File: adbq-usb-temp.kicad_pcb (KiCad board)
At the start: 4 copper layers, 0 parts

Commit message: pcb: import footprints from schematic
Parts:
- added AE1: Antenna, RF_Antenna:Johanson_2450AT18x100, F.Cu at (155.2, 88.0)
- added C1: 1u, Capacitor_SMD:C_0402_1005Metric, F.Cu at (137.8, 93.2)
- added C10: 0u1, Capacitor_SMD:C_0402_1005Metric, F.Cu at (140.7, 97.1)
- added C11: 0u1, Capacitor_SMD:C_0402_1005Metric, F.Cu at (140.7, 99.1)
- added C13: 10n, Capacitor_SMD:C_0402_1005Metric, F.Cu at (140.7, 101.1)
- added C14: 1u, Capacitor_SMD:C_0402_1005Metric, F.Cu at (140.7, 103.1)
- added C15: 1u, Capacitor_SMD:C_0402_1005Metric, F.Cu at (143.5, 93.2)
- added C16: 0u1, Capacitor_SMD:C_0402_1005Metric, F.Cu at (143.5, 95.2)
- added C17: 0u1, Capacitor_SMD:C_0402_1005Metric, F.Cu at (143.5, 97.1)
- added C18: 0u1, Capacitor_SMD:C_0402_1005Metric, F.Cu at (143.5, 99.1)
- added C2: 10u, Capacitor_SMD:C_0402_1005Metric, F.Cu at (137.8, 95.2)
- added C23: 12p, Capacitor_SMD:C_0402_1005Metric, F.Cu at (143.5, 101.1)
- added C25: 12p, Capacitor_SMD:C_0402_1005Metric, F.Cu at (143.5, 103.1)
- added C28: 1p2, Capacitor_SMD:C_0402_1005Metric, F.Cu at (146.4, 93.2)
- added C29: 1p2, Capacitor_SMD:C_0402_1005Metric, F.Cu at (146.4, 95.2)
- added C3: 10u, Capacitor_SMD:C_0402_1005Metric, F.Cu at (137.8, 97.1)
- added C4: 10u, Capacitor_SMD:C_0402_1005Metric, F.Cu at (137.8, 99.1)
- added C48: 0u1, Capacitor_SMD:C_0402_1005Metric, F.Cu at (146.4, 97.1)
- added C5: 100p, Capacitor_SMD:C_0402_1005Metric, F.Cu at (137.8, 101.1)
- added C52: 1p, Capacitor_SMD:C_0402_1005Metric, F.Cu at (146.4, 99.1)
- added C6: 0u1, Capacitor_SMD:C_0402_1005Metric, F.Cu at (137.8, 103.1)
- added C8: 10u, Capacitor_SMD:C_0402_1005Metric, F.Cu at (140.7, 93.2)
- added C9: 1u, Capacitor_SMD:C_0402_1005Metric, F.Cu at (140.7, 95.2)
- added D1: H5VU10U, Pers:Diode_DFN1006, F.Cu at (157.4, 103.7)
- added D2: H5VU10U, Pers:Diode_DFN1006, F.Cu at (157.4, 105.7)
- added D3: H5VU10U, Pers:Diode_DFN1006, F.Cu at (157.4, 107.7)
- added J4: USB_C_Receptacle_USB2.0_14P, Connector_USB:USB_C_Receptacle_HRO_TYPE-C-31-M-12, F.Cu at (153.7, 98.0)
- added JP1: Jumper_2_Open, Jumper:SolderJumper-2_P1.3mm_Open_RoundedPad1.0x1.5mm, F.Cu at (154.5, 80.9)
- added L1: 0u47, Pers:TDK_TFM201610ALC, F.Cu at (127.0, 109.7)
- added L2: 2n7, Inductor_SMD:L_0402_1005Metric, F.Cu at (126.2, 93.2)
- added L3: 24n, Inductor_SMD:L_0402_1005Metric, F.Cu at (126.2, 95.2)
- added L4: 2n7, Inductor_SMD:L_0402_1005Metric, F.Cu at (126.2, 97.2)
- added L6: 3n9, Inductor_SMD:L_0402_1005Metric, F.Cu at (126.2, 99.2)
- added L7: 2n7, Inductor_SMD:L_0402_1005Metric, F.Cu at (126.2, 101.2)
- added Q1: Q_NMOS, Package_TO_SOT_SMD:SOT-323_SC-70, F.Cu at (150.1, 104.7)
- added Q2: Q_NMOS, Package_TO_SOT_SMD:SOT-323_SC-70, F.Cu at (150.1, 108.6)
- added Q3: Q_NMOS, Package_TO_SOT_SMD:SOT-323_SC-70, F.Cu at (150.1, 112.4)
- added R1: 10k, Resistor_SMD:R_0402_1005Metric, F.Cu at (126.2, 103.2)
- added R10: 22, Resistor_SMD:R_0402_1005Metric, F.Cu at (129.1, 103.2)
- added R11: 510, Resistor_SMD:R_0402_1005Metric, F.Cu at (129.1, 105.2)
- added R12: 5k1, Resistor_SMD:R_0402_1005Metric, F.Cu at (129.1, 107.1)
- added R13: 5k1, Resistor_SMD:R_0402_1005Metric, F.Cu at (132.0, 93.2)
- added R14: 22, Resistor_SMD:R_0402_1005Metric, F.Cu at (132.0, 95.2)
- added R15: 510, Resistor_SMD:R_0402_1005Metric, F.Cu at (132.0, 97.2)
- added R16: 150, Resistor_SMD:R_0402_1005Metric, F.Cu at (132.0, 99.2)
- added R17: 150, Resistor_SMD:R_0402_1005Metric, F.Cu at (132.0, 101.2)
- added R18: 150, Resistor_SMD:R_0402_1005Metric, F.Cu at (132.0, 103.2)
- added R19: 150, Resistor_SMD:R_0402_1005Metric, F.Cu at (132.0, 105.2)
- added R2: 10k, Resistor_SMD:R_0402_1005Metric, F.Cu at (126.2, 105.2)
- added R20: 150, Resistor_SMD:R_0402_1005Metric, F.Cu at (132.0, 107.1)
- added R21: 150, Resistor_SMD:R_0402_1005Metric, F.Cu at (134.9, 93.2)
- added R22: 150, Resistor_SMD:R_0402_1005Metric, F.Cu at (134.9, 95.2)
- added R23: 150, Resistor_SMD:R_0402_1005Metric, F.Cu at (134.9, 97.2)
- added R24: 10k, Resistor_SMD:R_0402_1005Metric, F.Cu at (134.9, 99.2)
- added R25: 20k, Resistor_SMD:R_0402_1005Metric, F.Cu at (134.9, 101.2)
- added R26: 20k, Resistor_SMD:R_0402_1005Metric, F.Cu at (134.9, 103.2)
- added R3: 10k, Resistor_SMD:R_0402_1005Metric, F.Cu at (126.2, 107.1)
- added R4: 430k, Resistor_SMD:R_0603_1608Metric, F.Cu at (126.7, 112.5)
- added R5: 100k, Resistor_SMD:R_0402_1005Metric, F.Cu at (129.1, 93.2)
- added R57: 10k, Resistor_SMD:R_0402_1005Metric, F.Cu at (134.9, 105.2)
- added R6: 510, Resistor_SMD:R_0402_1005Metric, F.Cu at (129.1, 95.2)
- added R7: 510, Resistor_SMD:R_0402_1005Metric, F.Cu at (129.1, 97.2)
- added R8: 510, Resistor_SMD:R_0402_1005Metric, F.Cu at (129.1, 99.2)
- added R9: 510, Resistor_SMD:R_0402_1005Metric, F.Cu at (129.1, 101.2)
- added SW1: SW_Push, Jumper:SolderJumper-2_P1.3mm_Open_RoundedPad1.0x1.5mm, F.Cu at (154.5, 84.5)
- added SW2: TestPoint, TestPoint:TestPoint_Pad_D1.5mm, F.Cu at (154.1, 104.5)
- added SW3: TestPoint, TestPoint:TestPoint_Pad_D1.5mm, F.Cu at (154.1, 108.0)
- added SW4: TestPoint, TestPoint:TestPoint_Pad_D1.5mm, F.Cu at (154.1, 111.6)
- added U1: ESP32-S3FH4R2, Package_DFN_QFN:QFN-56-1EP_7x7mm_P0.4mm_EP5.6x5.6mm, F.Cu at (141.4, 108.7)
- added U14: TMP117AIDRV, Package_SON:WSON-6-1EP_2x2mm_P0.65mm_EP1x1.6mm, F.Cu at (150.4, 84.7)
- added U2: TPS6282x, Pers:Texas_VSON-6_1.5x1.5mm_P0.5mm_DMQ0006A, F.Cu at (157.6, 110.5)
- added U3: XL-SB2301SRWC, Pers:XL-SB2301SRWC, F.Cu at (136.7, 85.7)
- added U4: TMP117AIDRV, Package_SON:WSON-6-1EP_2x2mm_P0.65mm_EP1x1.6mm, F.Cu at (150.4, 81.0)
- added Y1: 48M, Crystal:Crystal_SMD_2016-4Pin_2.0x1.6mm, F.Cu at (131.3, 110.0)

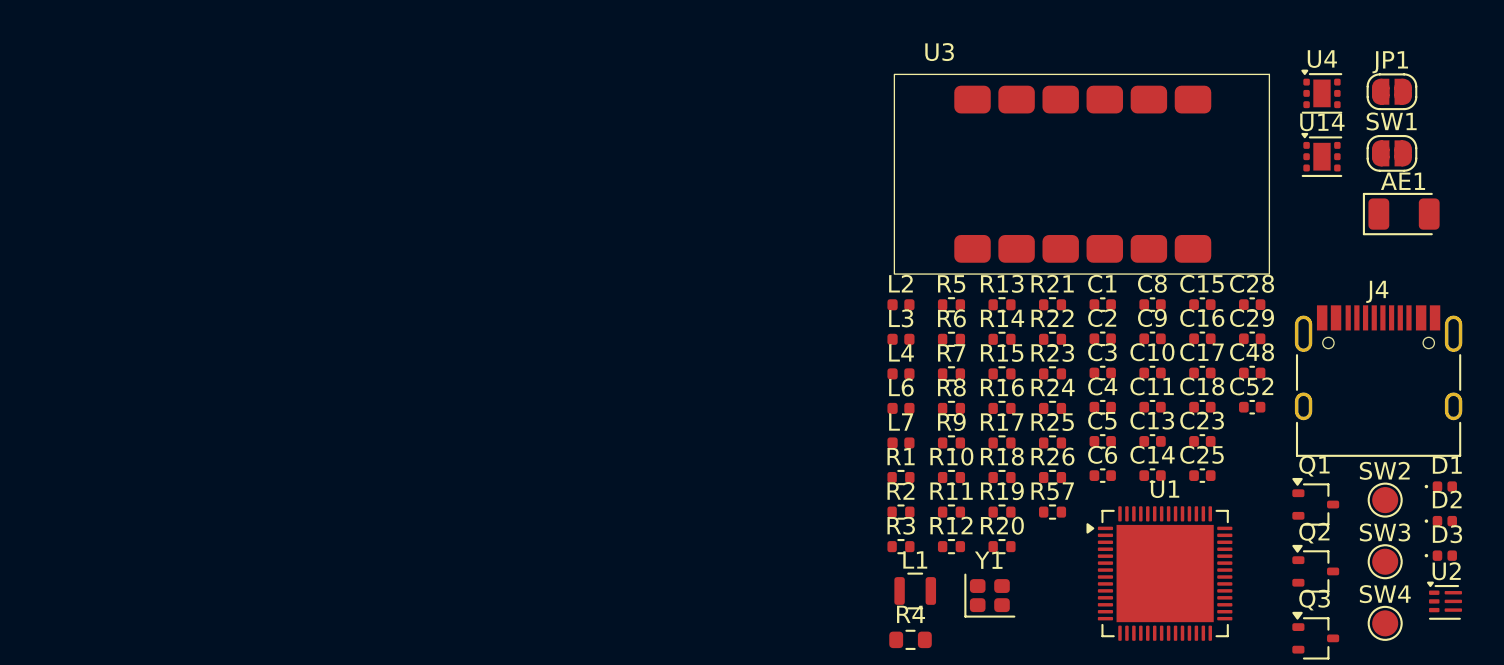
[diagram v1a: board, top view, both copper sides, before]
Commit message: pcb: add missing 3d models
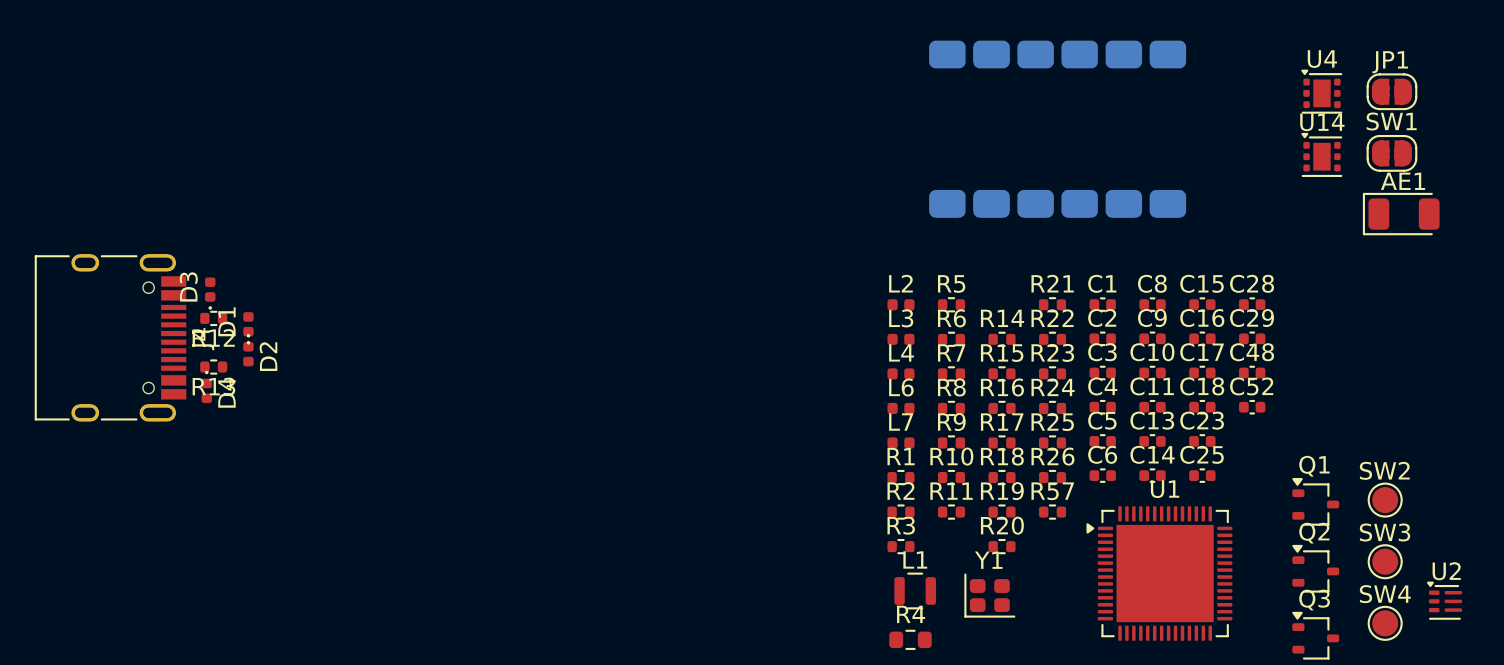
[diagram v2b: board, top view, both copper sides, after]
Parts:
- added D4: H5VU10U, Pers:Diode_DFN1006, F.Cu at (86.2, 98.1)
- U3: moved to B.Cu
- moved J4 73.5 mm to (80.2, 95.1), turned to -90 degrees
- moved D3 72.7 mm to (86.4, 92.4), turned to 90 degrees
- moved D2 69.5 mm to (88.6, 96.0), turned to -90 degrees
- moved D1 69.5 mm to (88.6, 94.4), turned to 90 degrees
- moved R13 45.5 mm to (86.6, 96.8), turned to 180 degrees
- moved R12 44.5 mm to (86.6, 94.0), turned to 180 degrees
- moved U3 2.97 mm to (135.2, 83.1), turned to 180 degrees

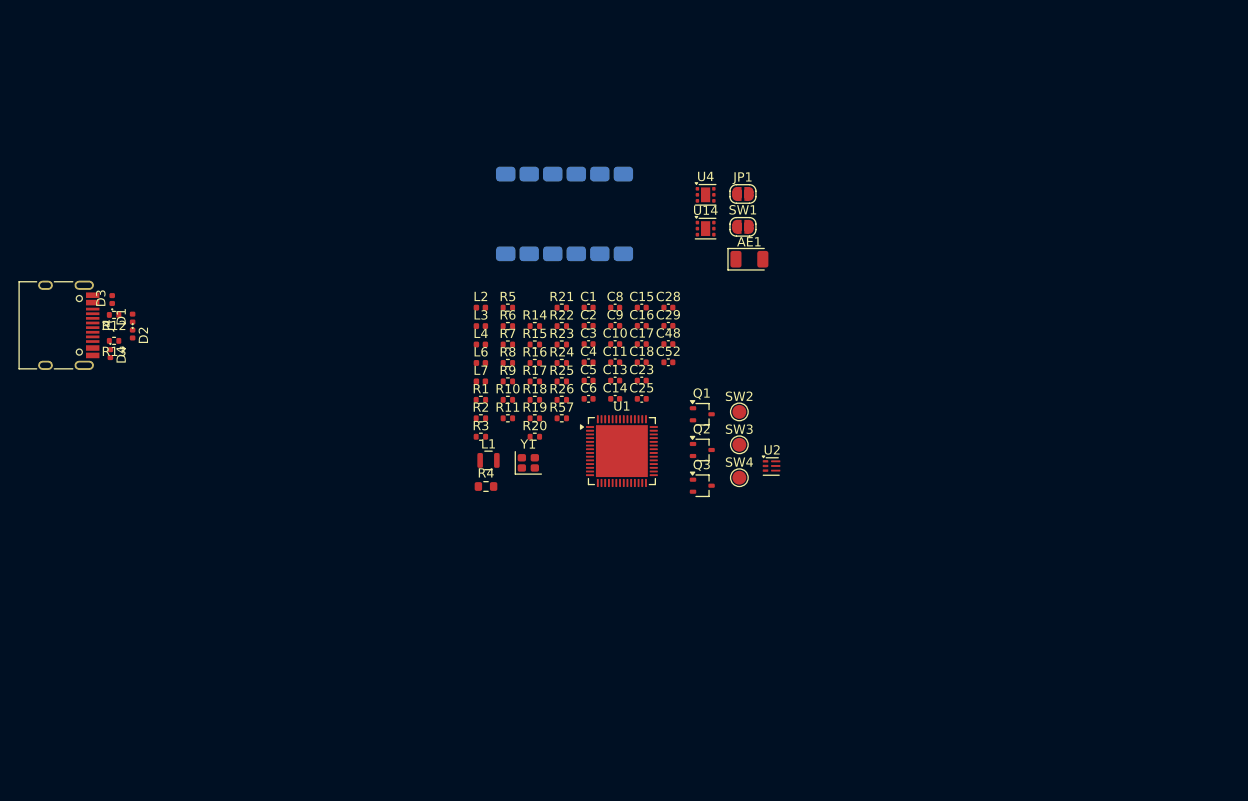
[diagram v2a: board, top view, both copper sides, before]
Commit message: pcb: inital rough placement
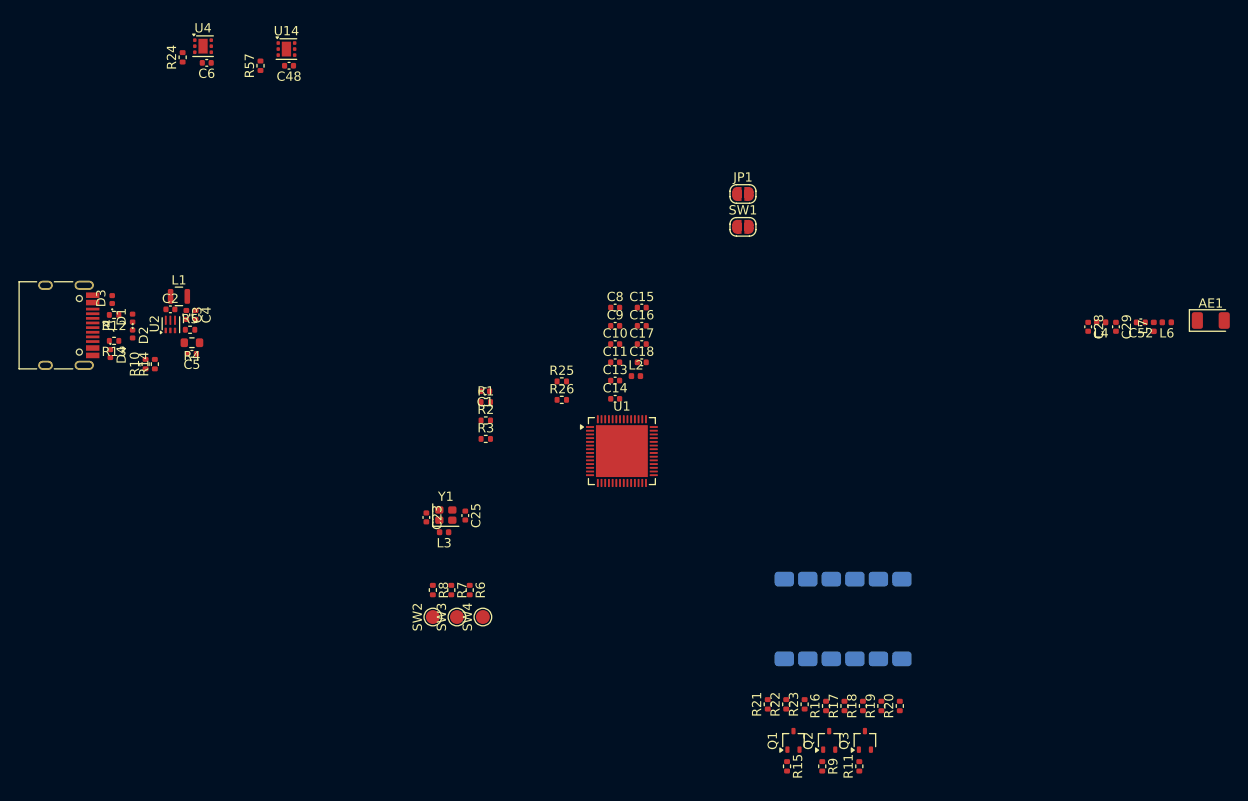
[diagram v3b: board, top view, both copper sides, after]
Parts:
- moved L6 74.1 mm to (200.2, 94.8), turned to 180 degrees
- moved L7 72.9 mm to (198.8, 95.3), turned to 90 degrees
- moved L4 67.0 mm to (193.1, 94.8), turned to 180 degrees
- moved U2 66.6 mm to (92.9, 95.0), turned to 90 degrees
- moved U4 56.6 mm to (96.2, 65.0)
- moved C6 54.9 mm to (96.6, 66.8), turned to 180 degrees
- moved R9 53.6 mm to (163.0, 142.7), turned to -90 degrees
- moved R11 53.4 mm to (167.0, 142.7), turned to 90 degrees
- moved U3 53.0 mm to (165.3, 126.8)
- moved R15 53.0 mm to (159.2, 142.7), turned to -90 degrees
- moved R24 52.6 mm to (94.0, 66.2), turned to 90 degrees
- moved C52 51.2 mm to (197.4, 94.8), turned to 180 degrees
- moved C48 50.8 mm to (105.5, 67.1), turned to 180 degrees
- moved AE1 50.2 mm to (204.9, 94.6)
- moved R57 50.0 mm to (102.4, 67.1), turned to 90 degrees
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
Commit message: pcb: layout refinement
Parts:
- SW2: moved to B.Cu
- moved C28 83.8 mm to (108.0, 90.9), turned to 90 degrees
- moved L4 83.8 mm to (109.4, 91.3)
- moved C29 83.4 mm to (111.4, 90.9), turned to 45 degrees
- moved L7 82.7 mm to (116.2, 90.8), turned to 0 degrees
- moved AE1 82.6 mm to (122.4, 90.8)
- moved L6 81.3 mm to (119.0, 90.8)
- moved C52 79.9 mm to (117.6, 91.2), turned to 90 degrees
- moved SW3 44.4 mm to (102.4, 87.6), turned to -90 degrees
- moved SW2 44.4 mm to (98.8, 88.2), turned to -90 degrees
- moved SW4 44.2 mm to (105.6, 87.6), turned to -90 degrees
- moved C6 39.8 mm to (116.2, 101.4)
- moved R24 39.8 mm to (113.6, 100.8)
- moved U4 39.8 mm to (115.8, 99.6)
- moved R6 39.6 mm to (103.6, 90.4), turned to 90 degrees
- moved U1 39.2 mm to (104.4, 95.6), turned to -90 degrees
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
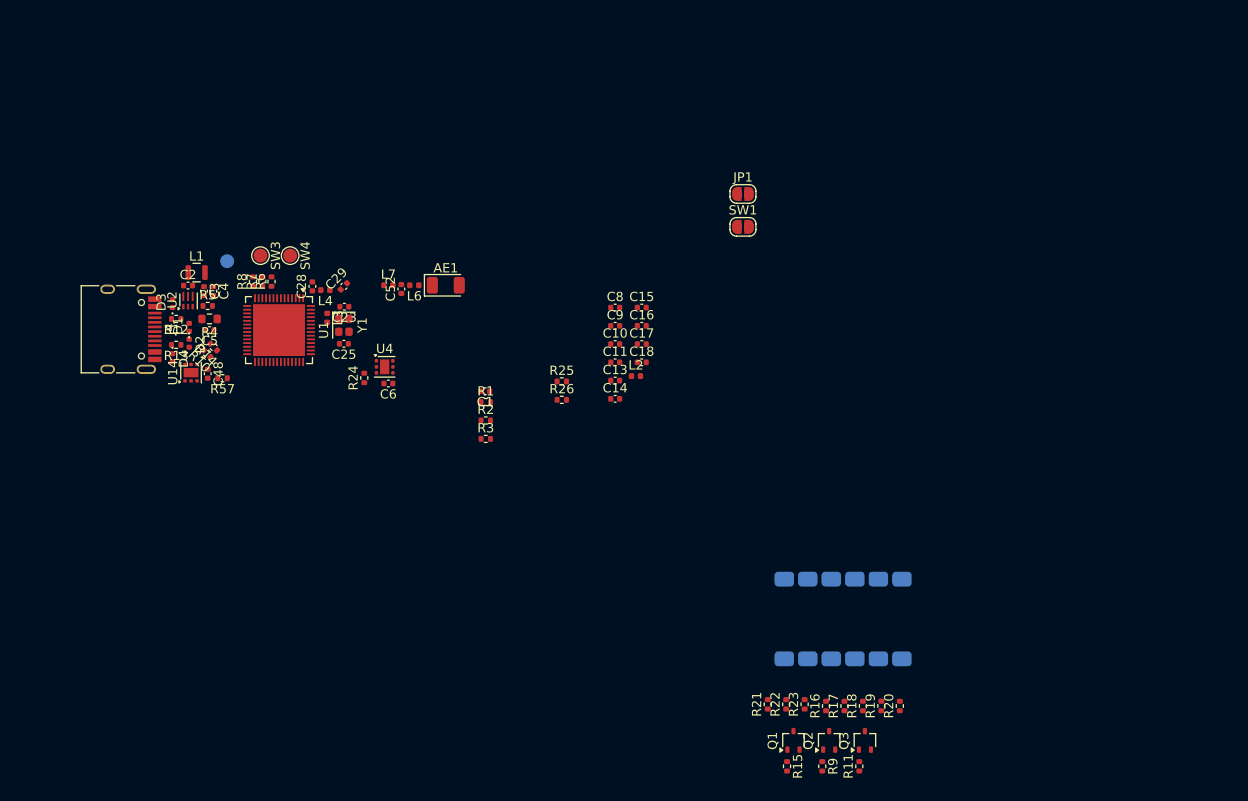
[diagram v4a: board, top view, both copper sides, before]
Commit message: pcb: area reduction
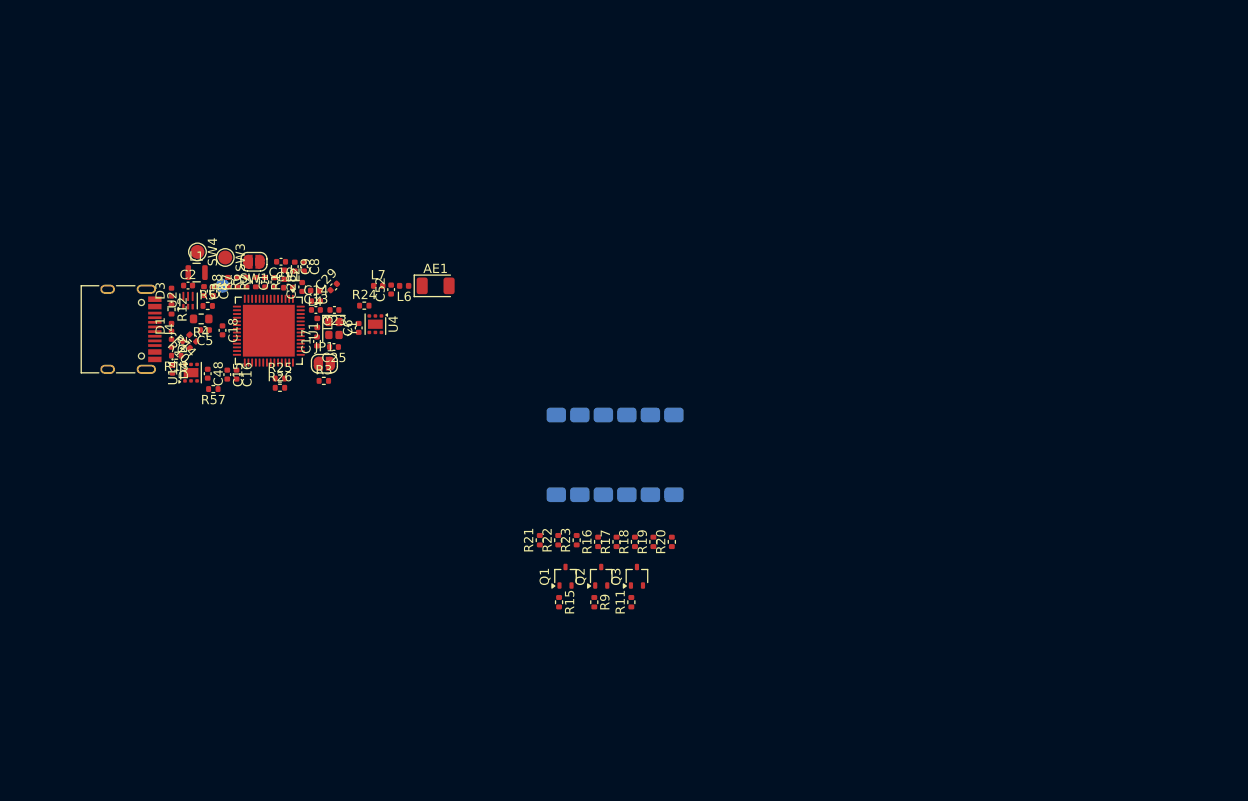
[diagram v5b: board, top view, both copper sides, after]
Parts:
- moved SW1 52.9 mm to (101.7, 88.3), turned to 180 degrees
- moved JP1 48.7 mm to (109.3, 99.3)
- moved C18 45.4 mm to (98.3, 95.7), turned to -90 degrees
- moved C15 45.3 mm to (98.8, 100.4), turned to -90 degrees
- moved C16 44.0 mm to (99.8, 100.4), turned to -90 degrees
- moved L2 39.5 mm to (105.0, 89.7), turned to -90 degrees
- moved C10 37.1 mm to (104.6, 88.3), turned to 180 degrees
- moved C11 36.2 mm to (105.4, 91.1)
- moved C9 35.2 mm to (106.1, 88.8), turned to -90 degrees
- moved C17 35.0 mm to (108.5, 96.9), turned to 90 degrees
- moved C14 34.0 mm to (108.4, 92.5)
- moved C8 33.9 mm to (107.1, 88.8), turned to -90 degrees
- moved C13 33.2 mm to (108.4, 93.5)
- moved R26 30.4 mm to (104.5, 101.9)
- moved R25 30.4 mm to (104.5, 100.9)
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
